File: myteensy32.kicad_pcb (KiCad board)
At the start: 2 copper layers, 2 parts, among them U1 MKL04Z32VLC4, U2 MK20DX256VLH7

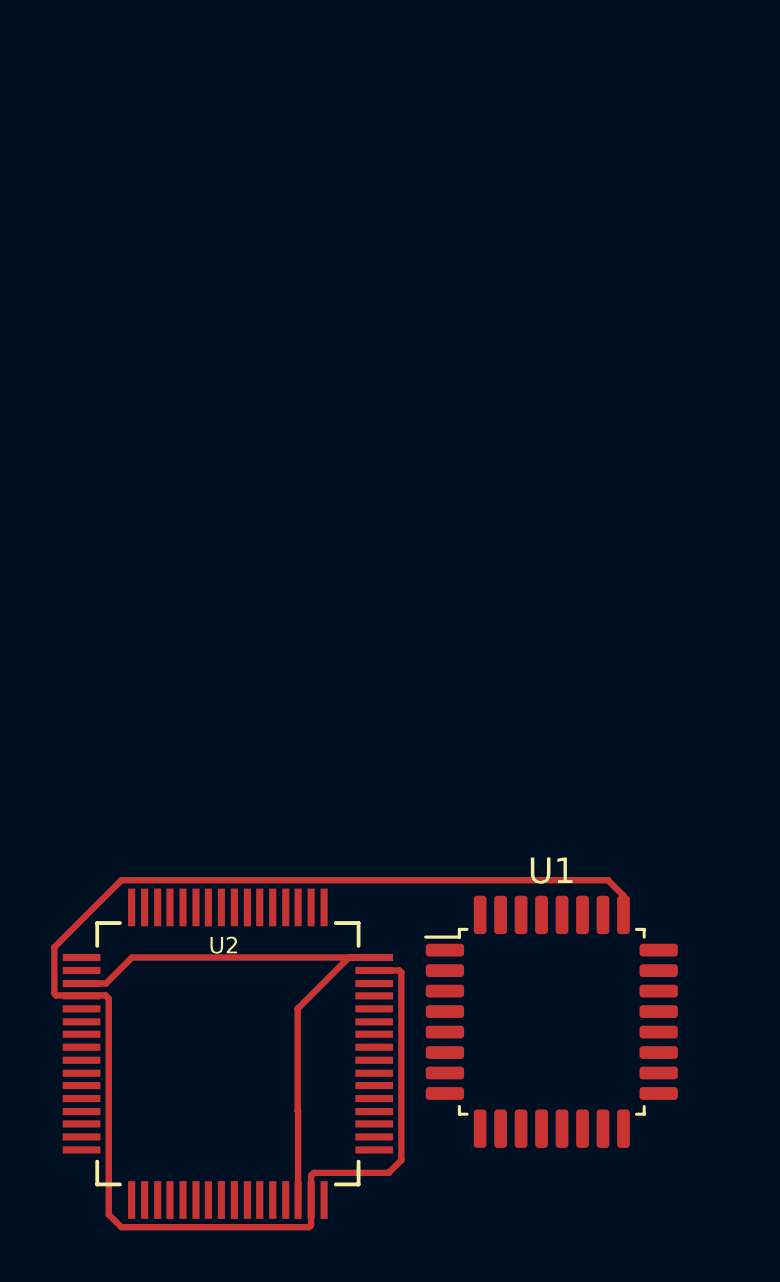
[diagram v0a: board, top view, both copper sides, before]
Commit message: usb,Crystal等周辺回路の追加
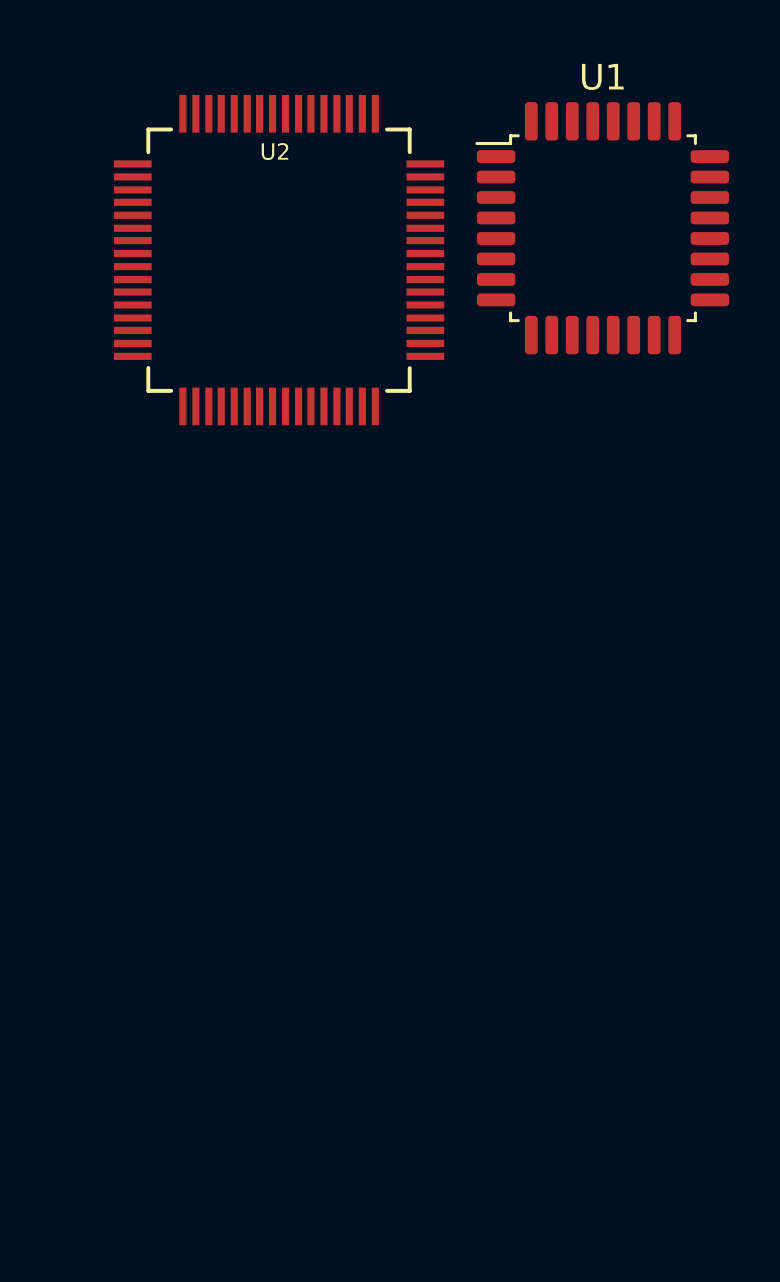
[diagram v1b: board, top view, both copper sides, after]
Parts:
- moved U2 31.1 mm to (143.5, 42.5)
- moved U1 31.1 mm to (156.1, 41.2)
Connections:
- net Net-(U1-Pad18) renamed /toProgramPushBtn
- U1 pad 10: Net-(U1-Pad10) -> /PTA1
- U1 pad 15: Net-(U1-Pad15) -> /PTA3
- U1 pad 16: Net-(U1-Pad16) -> /PTA0
- U1 pad 17: Net-(U1-Pad17) -> /PTA2
- U1 pad 25: Net-(U1-Pad25) -> /RESET
- U1 pad 3: Net-(U1-Pad3) -> +3V3
- U1 pad 4: Net-(U1-Pad4) -> +3V3
- U1 pad 5: Net-(U1-Pad5) -> GND
- U1 pad 6: Net-(U1-Pad6) -> GND
- U1 pad 8: Net-(U1-Pad8) -> /RESET
- U2 pad 22: Net-(U2-Pad22) -> /PTA0
- U2 pad 23: Net-(U2-Pad23) -> /PTA1
- U2 pad 24: Net-(U2-Pad24) -> /PTA2
- U2 pad 25: Net-(U2-Pad25) -> /PTA3
- U2 pad 31: Net-(U1-Pad25) -> Net-(U2-Pad31)
- U2 pad 34: Net-(U2-Pad34) -> /RESET
- U2 pad 4: Net-(U1-Pad25) -> Net-(U2-Pad31)
- U2 pad 47: Net-(U1-Pad25) -> Net-(U2-Pad31)
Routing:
- net Net-(U1-Pad25): track 59.1 -> 0.00 mm
- net Net-(U2-Pad3): track 23.1 -> 0.00 mm

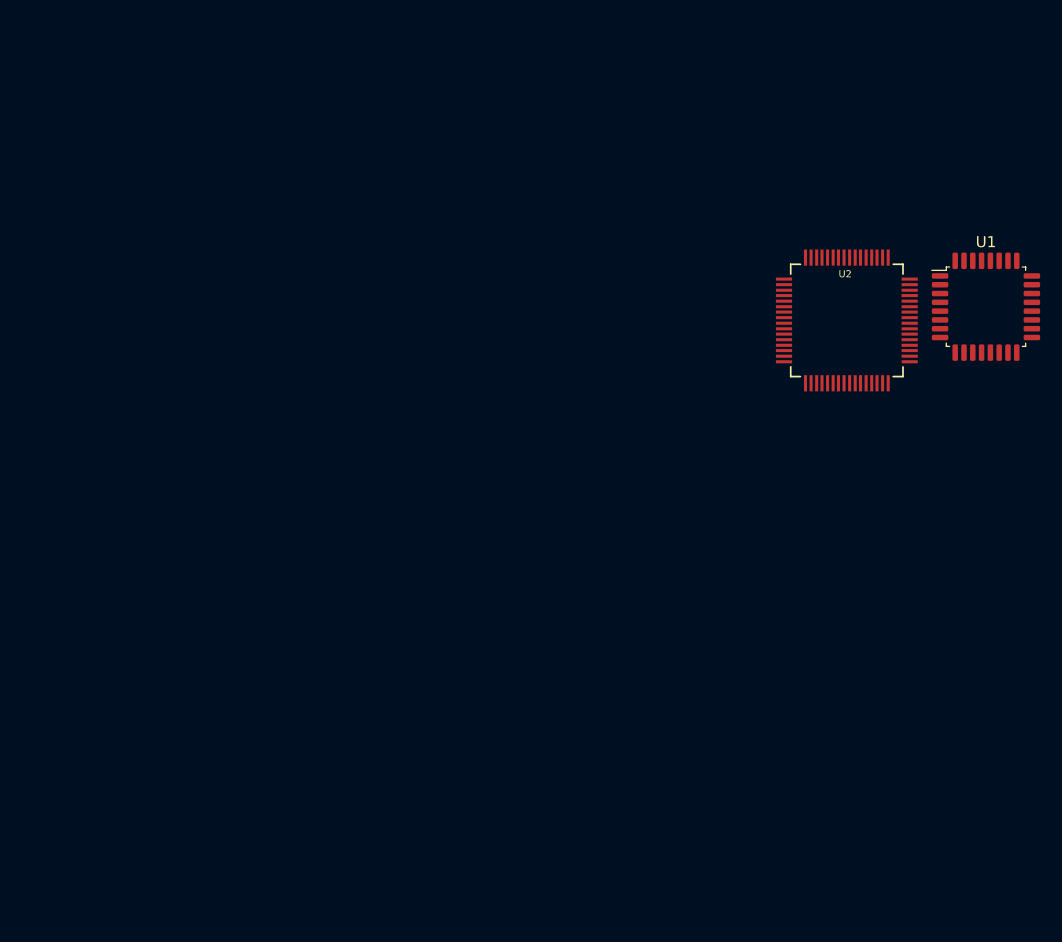
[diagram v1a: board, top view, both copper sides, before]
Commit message: とりあえず全部の素子にフットプリントを割り当てて大きさの余裕を見る。
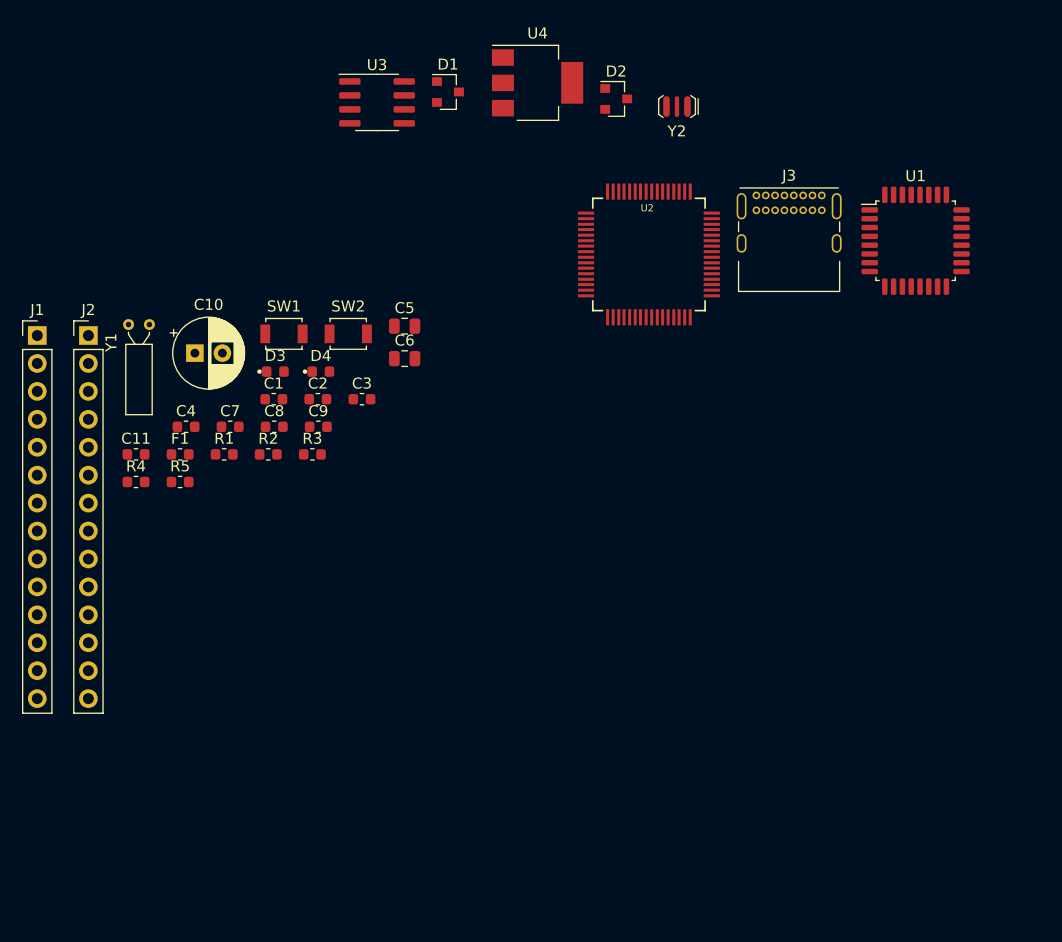
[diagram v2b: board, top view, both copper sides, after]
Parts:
- added C1: 0.1u, Capacitor_SMD:C_0603_1608Metric, F.Cu at (91.3, 49.6)
- added C10: 50uF(ESR<0.5ohm), Capacitor_THT:CP_Radial_D6.3mm_P2.50mm, F.Cu at (84.2, 45.4)
- added C11: 0.1u, Capacitor_SMD:C_0603_1608Metric, F.Cu at (78.8, 54.6)
- added C2: 0.1u, Capacitor_SMD:C_0603_1608Metric, F.Cu at (95.3, 49.6)
- added C3: 0.1u, Capacitor_SMD:C_0603_1608Metric, F.Cu at (99.4, 49.6)
- added C4: 0.1u, Capacitor_SMD:C_0603_1608Metric, F.Cu at (83.4, 52.1)
- added C5: 2.2u, Capacitor_SMD:C_0805_2012Metric, F.Cu at (103.2, 43.0)
- added C6: 2.2u, Capacitor_SMD:C_0805_2012Metric, F.Cu at (103.2, 45.9)
- added C7: 0.1u, Capacitor_SMD:C_0603_1608Metric, F.Cu at (87.4, 52.1)
- added C8: 0.1u, Capacitor_SMD:C_0603_1608Metric, F.Cu at (91.4, 52.1)
- added C9: 0.1u, Capacitor_SMD:C_0603_1608Metric, F.Cu at (95.4, 52.1)
- added D1: BAT54C, Package_TO_SOT_SMD:SOT-23, F.Cu at (107.2, 21.7)
- added D2: BAT54C, Package_TO_SOT_SMD:SOT-23, F.Cu at (122.5, 22.3)
- added D3: LED, mylib:LED_1608_point, F.Cu at (91.5, 47.1)
- added D4: LED, mylib:LED_1608_point, F.Cu at (95.6, 47.1)
- added F1: Itrip:0.75A, Fuse:Fuse_0603_1608Metric, F.Cu at (82.8, 54.6)
- added J1: Conn_01x14_Male, Connector_PinHeader_2.54mm:PinHeader_1x14_P2.54mm_Vertical, F.Cu at (69.8, 43.8)
- added J2: Conn_01x14_Male, Connector_PinHeader_2.54mm:PinHeader_1x14_P2.54mm_Vertical, F.Cu at (74.5, 43.8)
- added J3: USB_C_Receptacle_USB2.0, Connector_USB:USB_C_Receptacle_GCT_USB4085, F.Cu at (135.2, 31.1)
- added R1: 470, Resistor_SMD:R_0603_1608Metric, F.Cu at (86.8, 54.6)
- added R2: 33, Resistor_SMD:R_0603_1608Metric, F.Cu at (90.8, 54.6)
- added R3: 33, Resistor_SMD:R_0603_1608Metric, F.Cu at (94.8, 54.6)
- added R4: R, Resistor_SMD:R_0603_1608Metric, F.Cu at (78.8, 57.1)
- added R5: R, Resistor_SMD:R_0603_1608Metric, F.Cu at (82.8, 57.1)
- added SW1: RESET, Button_Switch_SMD:SW_SPST_B3U-1000P, F.Cu at (92.3, 43.7)
- added SW2: PROG, Button_Switch_SMD:SW_SPST_B3U-1000P, F.Cu at (98.1, 43.7)
- added U3: MCP2562-E-SN, Package_SO:SOIC-8_3.9x4.9mm_P1.27mm, F.Cu at (100.7, 22.6)
- added U4: LT1117-3.3, Package_TO_SOT_SMD:SOT-223-3_TabPin2, F.Cu at (115.3, 20.8)
- added Y1: 32.768kHz, Crystal:Crystal_DS26_D2.0mm_L6.0mm_Horizontal, F.Cu at (78.1, 42.8)
- added Y2: 16MHz, mylib:CSTCE16M0V53-R0, F.Cu at (128.0, 23.0)
- moved U2 19.0 mm to (125.5, 36.5)
- moved U1 8.77 mm to (149.7, 35.2)
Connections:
- U1 pad 18: /toProgramPushBtn -> /ProgramModeBtn
- U2 pad 13: Net-(U2-Pad13) -> +3V3
- U2 pad 15: Net-(U2-Pad15) -> GND
- U2 pad 16: Net-(U2-Pad16) -> GND
- U2 pad 28: Net-(U2-Pad28) -> /CAN_TX
- U2 pad 29: Net-(U2-Pad29) -> /CAN_RX
- U2 pad 3: Net-(U2-Pad3) -> +3V3
- U2 pad 30: Net-(U2-Pad3) -> +3V3
- U2 pad 31: Net-(U2-Pad31) -> GND
- U2 pad 4: Net-(U2-Pad31) -> GND
- U2 pad 47: Net-(U2-Pad31) -> GND
- U2 pad 48: Net-(U2-Pad3) -> +3V3
- U2 pad 50: Net-(U2-Pad50) -> /INTERNAL_LED
- U2 pad 7: Net-(U2-Pad7) -> +3V3

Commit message: teensy3.2のサイズに収めようとしたけどかなり難しい
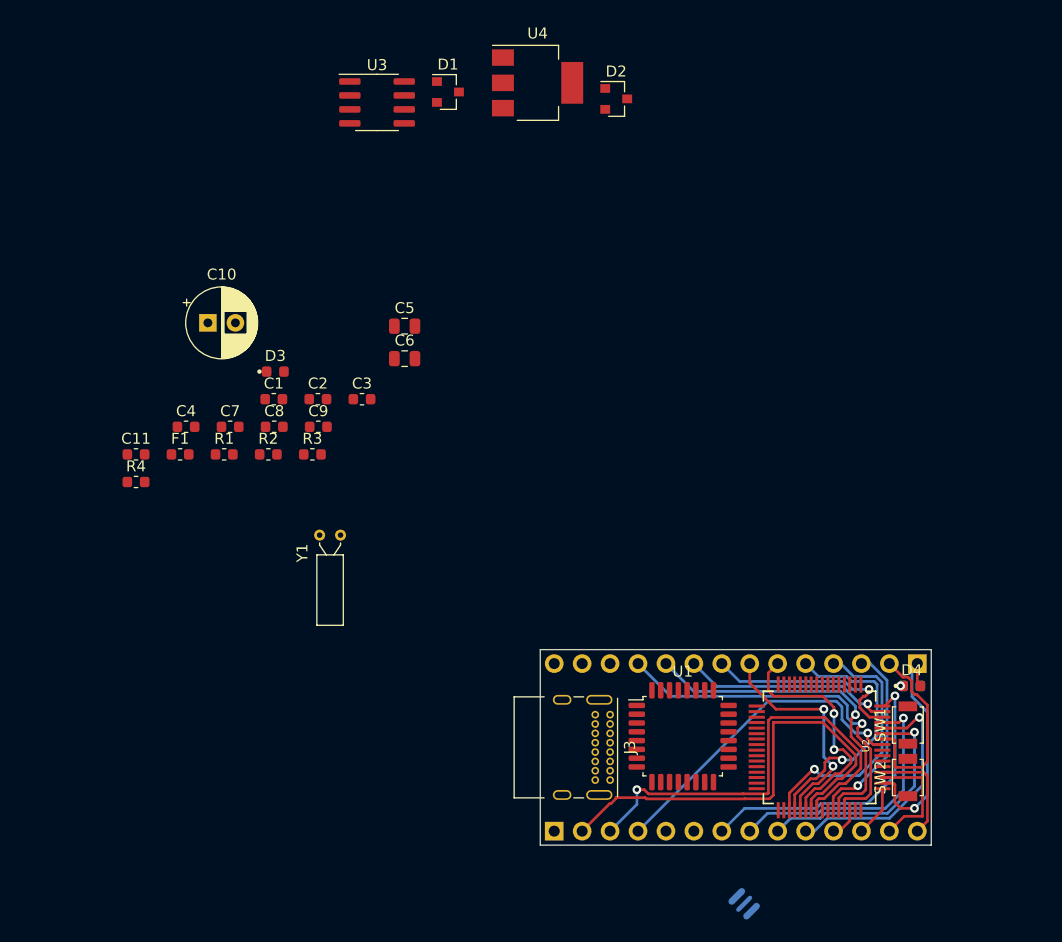
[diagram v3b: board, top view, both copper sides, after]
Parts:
- J1, J2, R5, Y2: moved to B.Cu
- moved J1 85.4 mm to (149.9, 73.7), turned to 90 degrees
- moved Y2 72.8 mm to (134.1, 95.5), turned to 135 degrees
- moved R5 69.1 mm to (149.4, 75.7)
- moved SW1 67.0 mm to (149.0, 79.2), turned to 90 degrees
- moved SW2 64.9 mm to (149.0, 84.0), turned to 90 degrees
- moved J2 61.9 mm to (116.8, 88.9), turned to 270 degrees
- moved D4 60.9 mm to (149.4, 75.7)
- moved U1 49.8 mm to (128.5, 80.3)
- moved J3 49.1 mm to (121.9, 78.3), turned to 270 degrees
- moved U2 47.4 mm to (141.0, 81.3), turned to 270 degrees
- moved Y1 25.9 mm to (95.5, 62.0)
- moved C10 3.00 mm to (85.3, 42.7)
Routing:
- net Net-(J2-Pad2): track 0.00 -> 41.5 mm
- net Net-(J2-Pad3): track 0.00 -> 40.9 mm, vias 0 -> 1
- net Net-(J1-Pad11): track 0.00 -> 33.9 mm, vias 0 -> 1
- net Net-(J1-Pad10): track 0.00 -> 31.0 mm, vias 0 -> 1
- net Net-(J2-Pad4): track 0.00 -> 29.8 mm, vias 0 -> 1
- net Net-(J2-Pad7): track 0.00 -> 26.6 mm, vias 0 -> 1
- net Net-(J2-Pad8): track 0.00 -> 24.2 mm, vias 0 -> 1
- net Net-(J1-Pad5): track 0.00 -> 23.6 mm, vias 0 -> 1
- net Net-(J1-Pad4): track 0.00 -> 23.5 mm, vias 0 -> 1
- net Net-(J2-Pad10): track 0.00 -> 22.4 mm, vias 0 -> 1
- net Net-(J1-Pad6): track 0.00 -> 22.1 mm, vias 0 -> 2
- net Net-(J2-Pad9): track 0.00 -> 22.0 mm, vias 0 -> 1
- net /INTERNAL_LED: track 0.00 -> 21.4 mm, vias 0 -> 1
- net Net-(J1-Pad7): track 0.00 -> 20.5 mm, vias 0 -> 2
- net Net-(J1-Pad9): track 0.00 -> 19.2 mm, vias 0 -> 1
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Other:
- board outline added: 35.6 x 17.8 mm

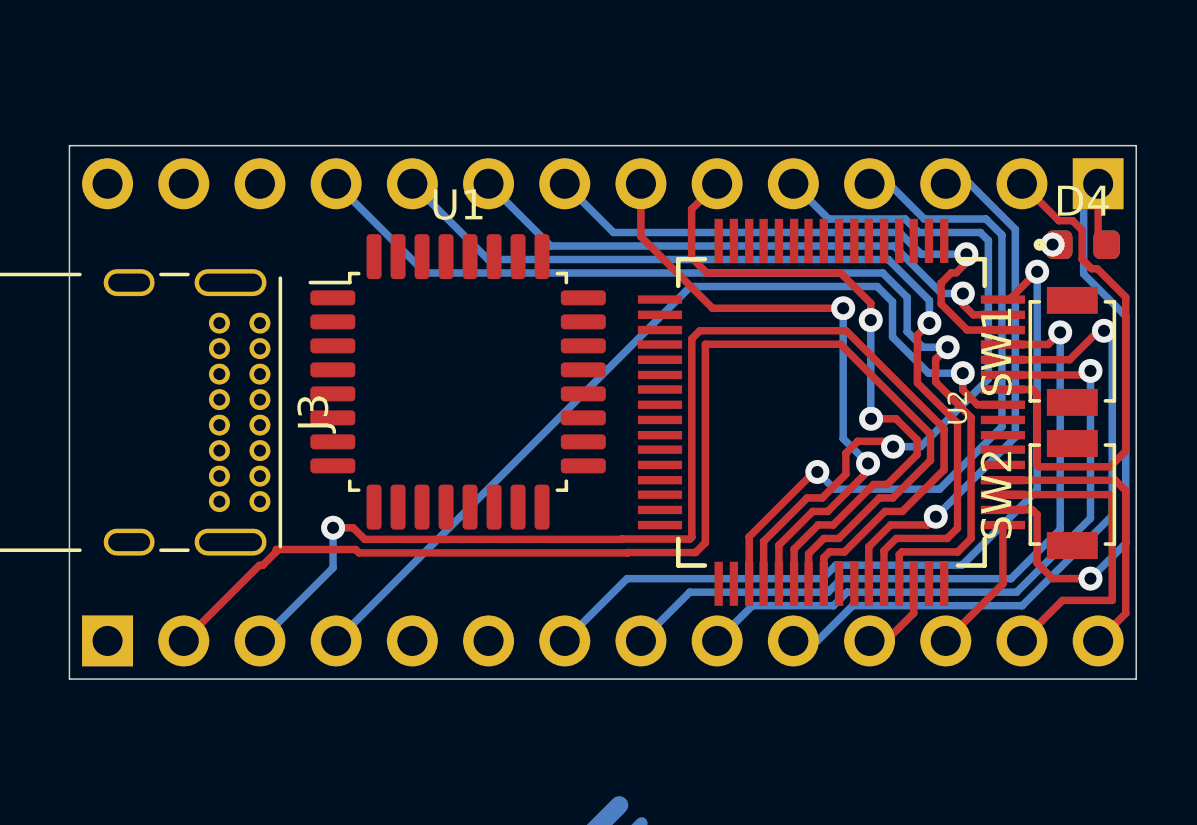
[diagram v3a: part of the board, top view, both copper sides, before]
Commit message: いったん配線を全削除
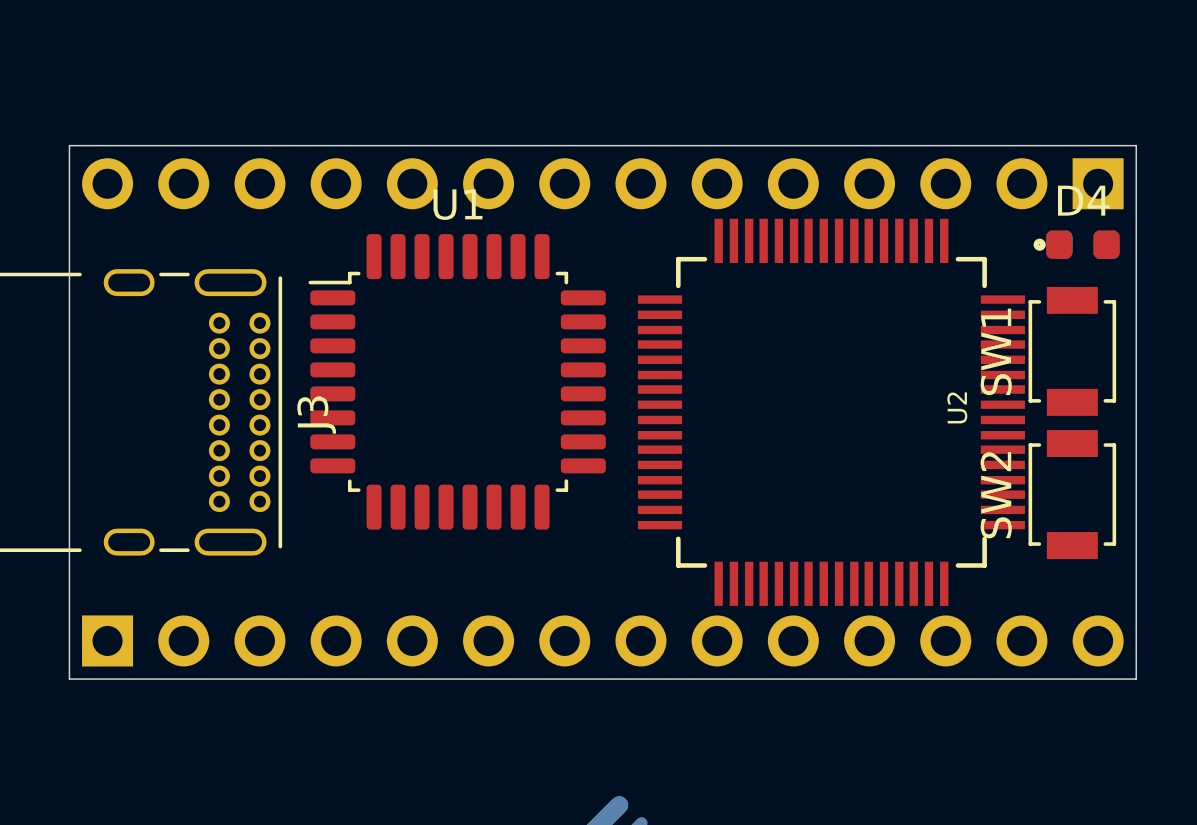
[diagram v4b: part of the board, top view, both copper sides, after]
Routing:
- net Net-(J2-Pad2): track 41.5 -> 0.00 mm
- net Net-(J2-Pad3): track 40.9 -> 0.00 mm, vias 1 -> 0
- net Net-(J1-Pad11): track 33.9 -> 0.00 mm, vias 1 -> 0
- net Net-(J1-Pad10): track 31.0 -> 0.00 mm, vias 1 -> 0
- net Net-(J2-Pad4): track 29.8 -> 0.00 mm, vias 1 -> 0
- net Net-(J2-Pad7): track 26.6 -> 0.00 mm, vias 1 -> 0
- net Net-(J2-Pad8): track 24.2 -> 0.00 mm, vias 1 -> 0
- net Net-(J1-Pad5): track 23.6 -> 0.00 mm, vias 1 -> 0
- net Net-(J1-Pad4): track 23.5 -> 0.00 mm, vias 1 -> 0
- net Net-(J2-Pad10): track 22.4 -> 0.00 mm, vias 1 -> 0
- net Net-(J1-Pad6): track 22.1 -> 0.00 mm, vias 2 -> 0
- net Net-(J2-Pad9): track 22.0 -> 0.00 mm, vias 1 -> 0
- net /INTERNAL_LED: track 21.4 -> 0.00 mm, vias 1 -> 0
- net Net-(J1-Pad7): track 20.5 -> 0.00 mm, vias 2 -> 0
- net Net-(J1-Pad9): track 19.2 -> 0.00 mm, vias 1 -> 0
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
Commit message: 配線幅を変えたら希望が見えてきた
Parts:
- Y2: moved to F.Cu
- moved Y2 8.89 mm to (133.9, 86.6), turned to 0 degrees
- moved SW2 1.00 mm to (149.5, 84.9)
- moved SW1 0.49 mm to (149.5, 79.3)
- moved D4 0.30 mm to (149.7, 75.7)
- moved R5 0.30 mm to (149.7, 75.7)
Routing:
- net Net-(J2-Pad7): track 0.00 -> 32.0 mm, vias 0 -> 1
- net Net-(J1-Pad11): track 0.00 -> 30.4 mm, vias 0 -> 1
- net Net-(J2-Pad2): track 0.00 -> 29.5 mm, vias 0 -> 1
- net Net-(J2-Pad4): track 0.00 -> 29.1 mm, vias 0 -> 1
- net Net-(J2-Pad3): track 0.00 -> 28.7 mm, vias 0 -> 1
- net Net-(J2-Pad8): track 0.00 -> 25.7 mm, vias 0 -> 1
- net Net-(J1-Pad10): track 0.00 -> 25.4 mm, vias 0 -> 1
- net Net-(J2-Pad9): track 0.00 -> 23.7 mm, vias 0 -> 1
- net Net-(J2-Pad10): track 0.00 -> 23.1 mm, vias 0 -> 1
- net Net-(J1-Pad8): track 0.00 -> 22.2 mm, vias 0 -> 1
- net /INTERNAL_LED: track 0.00 -> 21.4 mm, vias 0 -> 1
- net Net-(J1-Pad9): track 0.00 -> 21.0 mm, vias 0 -> 1
- net Net-(J1-Pad4): track 0.00 -> 17.5 mm, vias 0 -> 1
- net /RESET: track 0.00 -> 17.3 mm, vias 0 -> 2
- net Net-(J1-Pad6): track 0.00 -> 16.0 mm, vias 0 -> 1
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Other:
- net class 0.2 added: clearance 0.2, trace_width 0.2, via_dia 0.8, via_drill 0.4
- net class 0.5 added: clearance 0.2, trace_width 0.5, via_dia 1.5, via_drill 0.9
- net class 1.0 added: clearance 0.2, trace_width 1, via_dia 4, via_drill 3.2
